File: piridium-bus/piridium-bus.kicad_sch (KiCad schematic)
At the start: 86 parts, among them J1 EPS, J2 INHIBITS, J3 MODEM UART, J4 ANT, J5 PAYLOAD, Q1 DMP3015LSSQ, Q2 Si4186DY, Q3 DMP3015LSSQ, Q4 Si4186DY, Q5 DMP3015LSSQ, Q6 DMP3015LSSQ, Q7 2N7002, Q8 DMP3015LSSQ, U1 LM1117-3.3, U2 MAX6369, U3 TPS54394RSAR, U4 INA180A3, U5 74HC126, U6 DS3232M, U7 MCP3208, U8 INA180A3

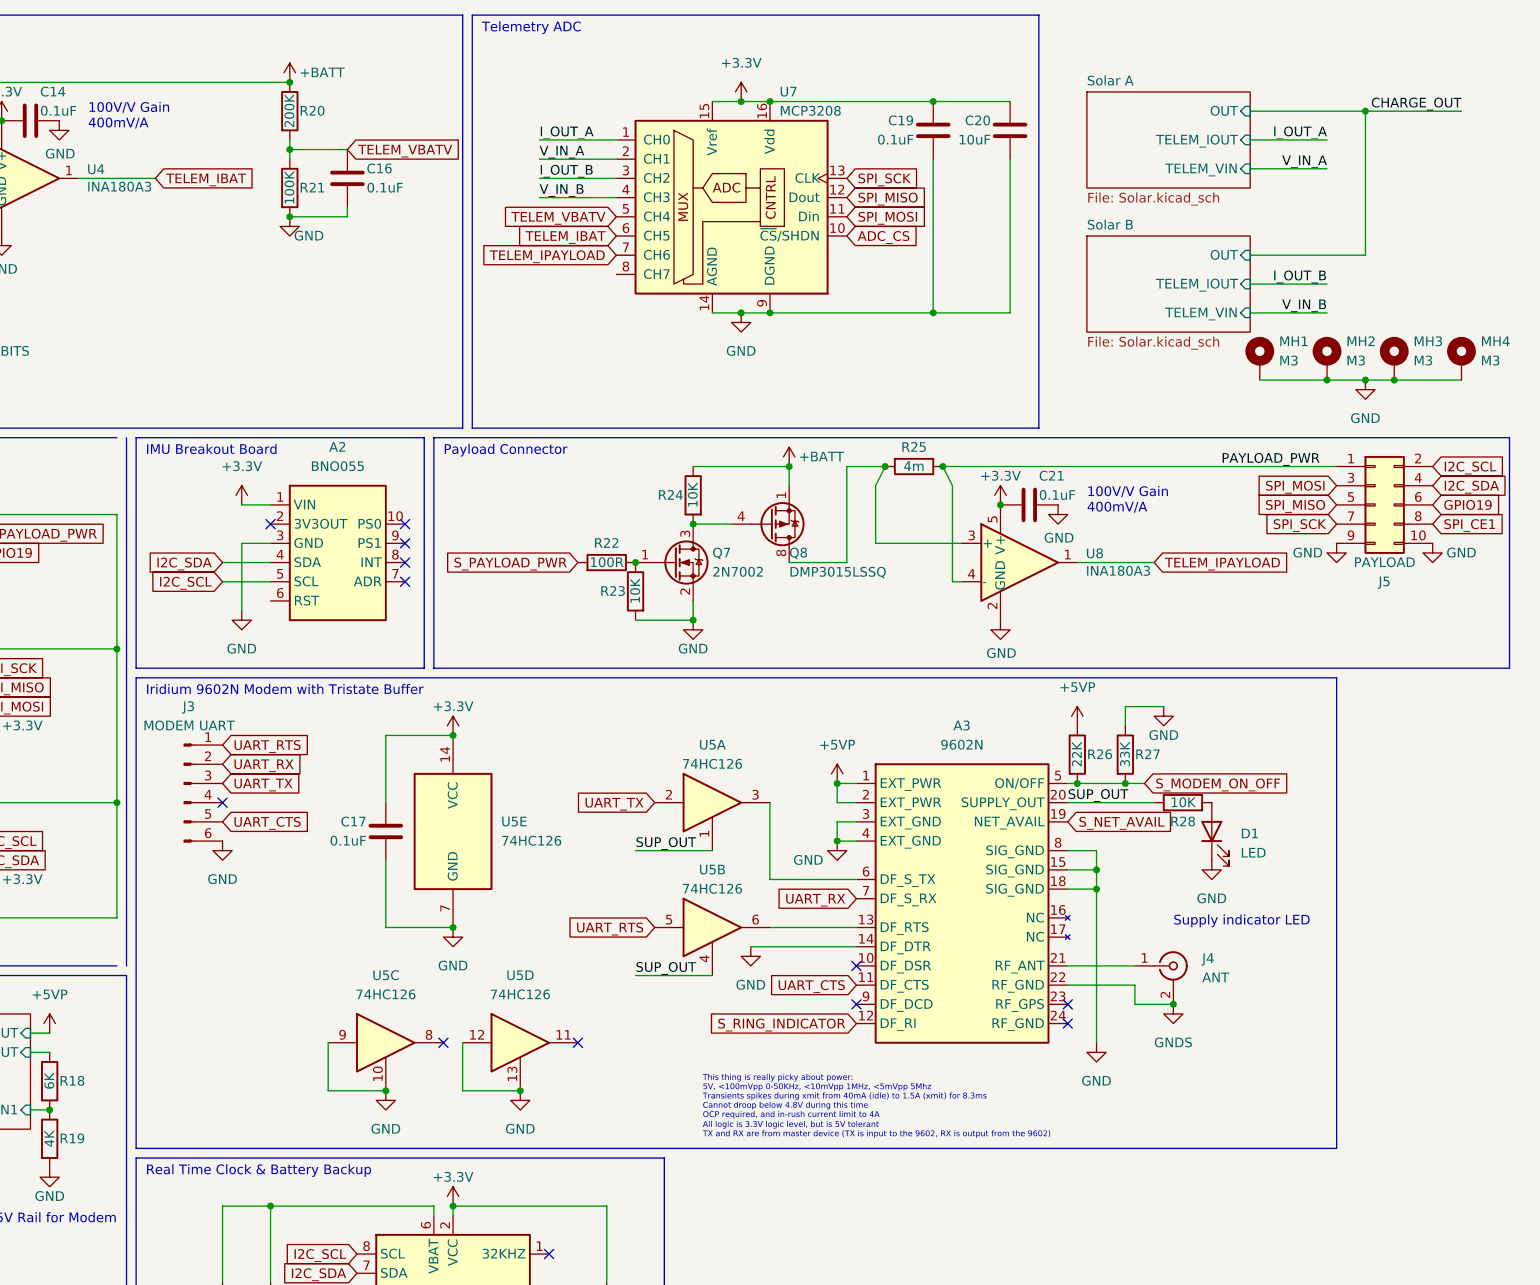
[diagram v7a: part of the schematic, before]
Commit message: mcp3208 constant reference
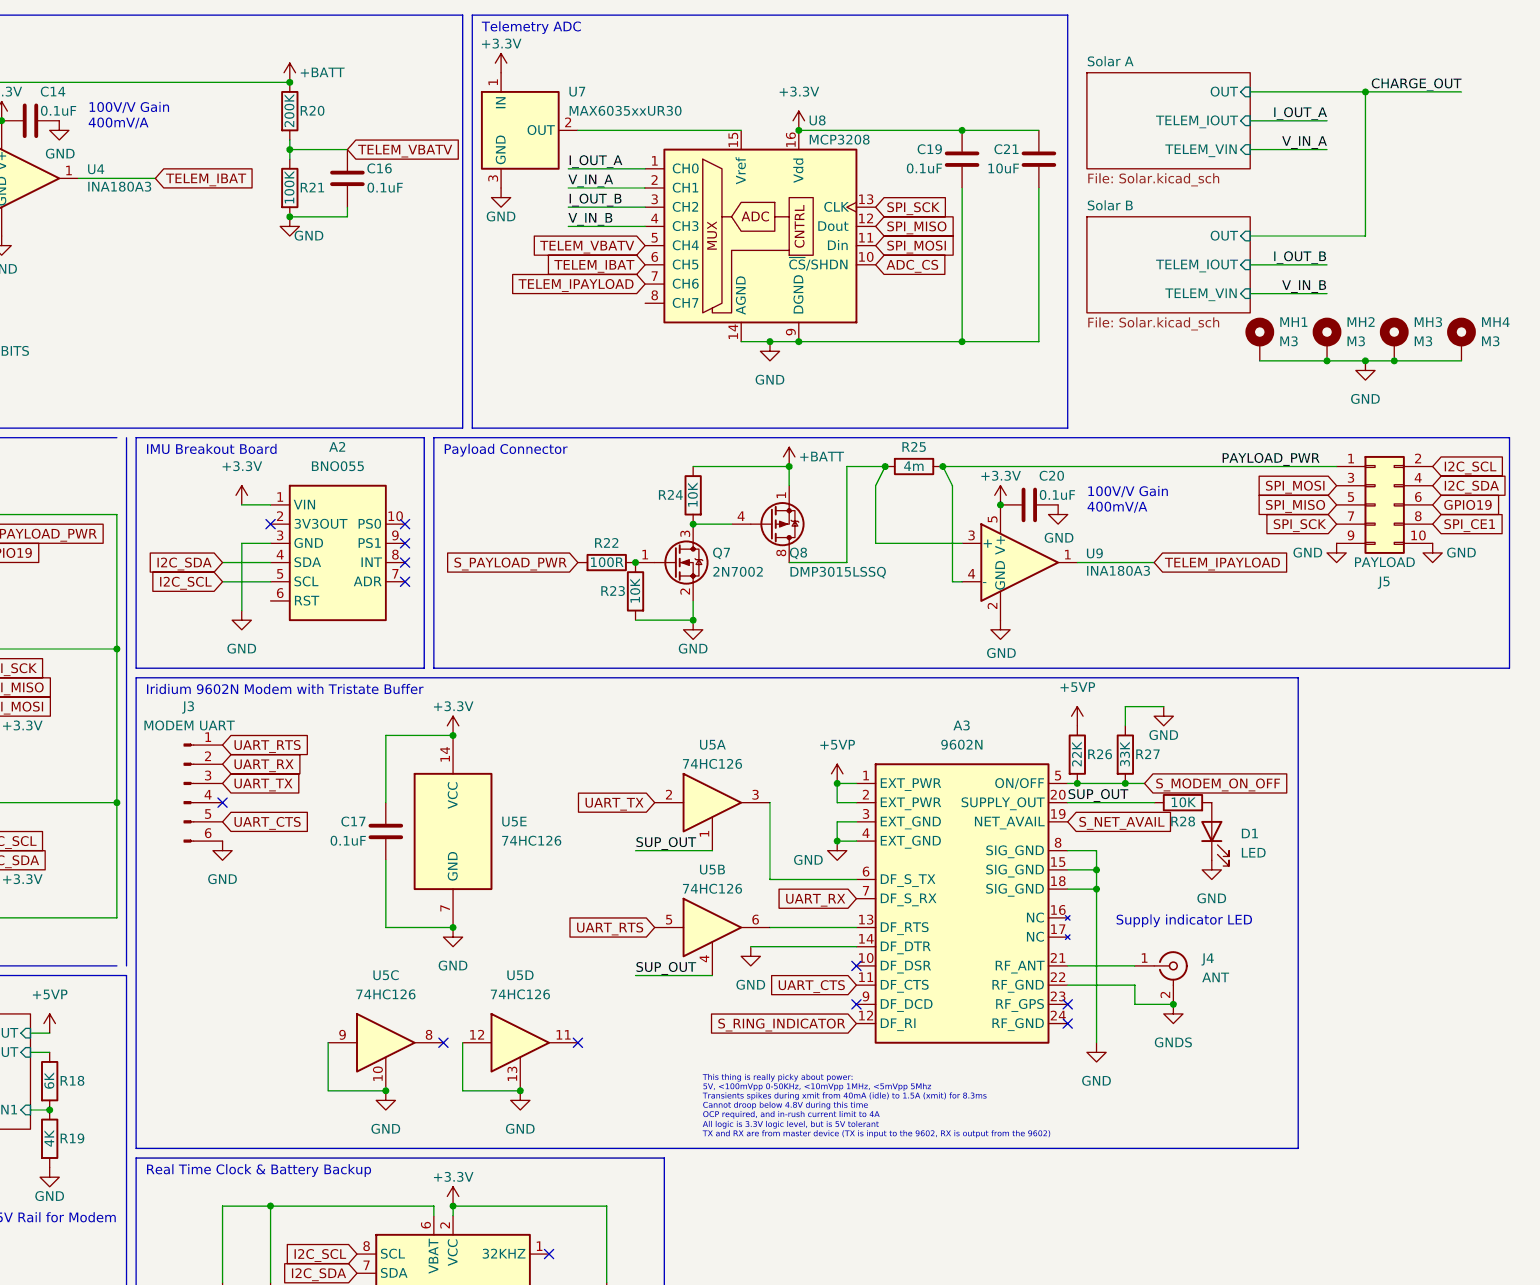
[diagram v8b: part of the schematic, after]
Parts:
- added U7: MAX6035xxUR30, Package_TO_SOT_SMD:SOT-23, symbol Reference_Voltage:MAX6035xxUR30
- R28: footprint Resistor_SMD:R_1206_3216Metric -> Resistor_SMD:R_0805_2012Metric
- renumbered C21 to C20, C20 to C21, U7 to U8, U8 to U9
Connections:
- net +3.3V: now also U7.1 (IN); no longer U8.15 (Vref)
- net GND: now also U7.3 (GND)
- new net: U7.2 (OUT), U8.15 (Vref)
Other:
- moved on the sheet: C19, C21, MH1, MH2, MH3, MH4, U8
